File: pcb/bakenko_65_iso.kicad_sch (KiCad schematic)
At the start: 43 parts, among them J1 JST SH 4-pin, J2 Conn_01x02_MountingPin, Q1 AO3407A, SW1 SW_Omron_B3FS, U1 XC6206P302MR-G, U2 NRF52840 aQFN73, U3 MCP73831, X1 32MHz, X2 32.768KHz

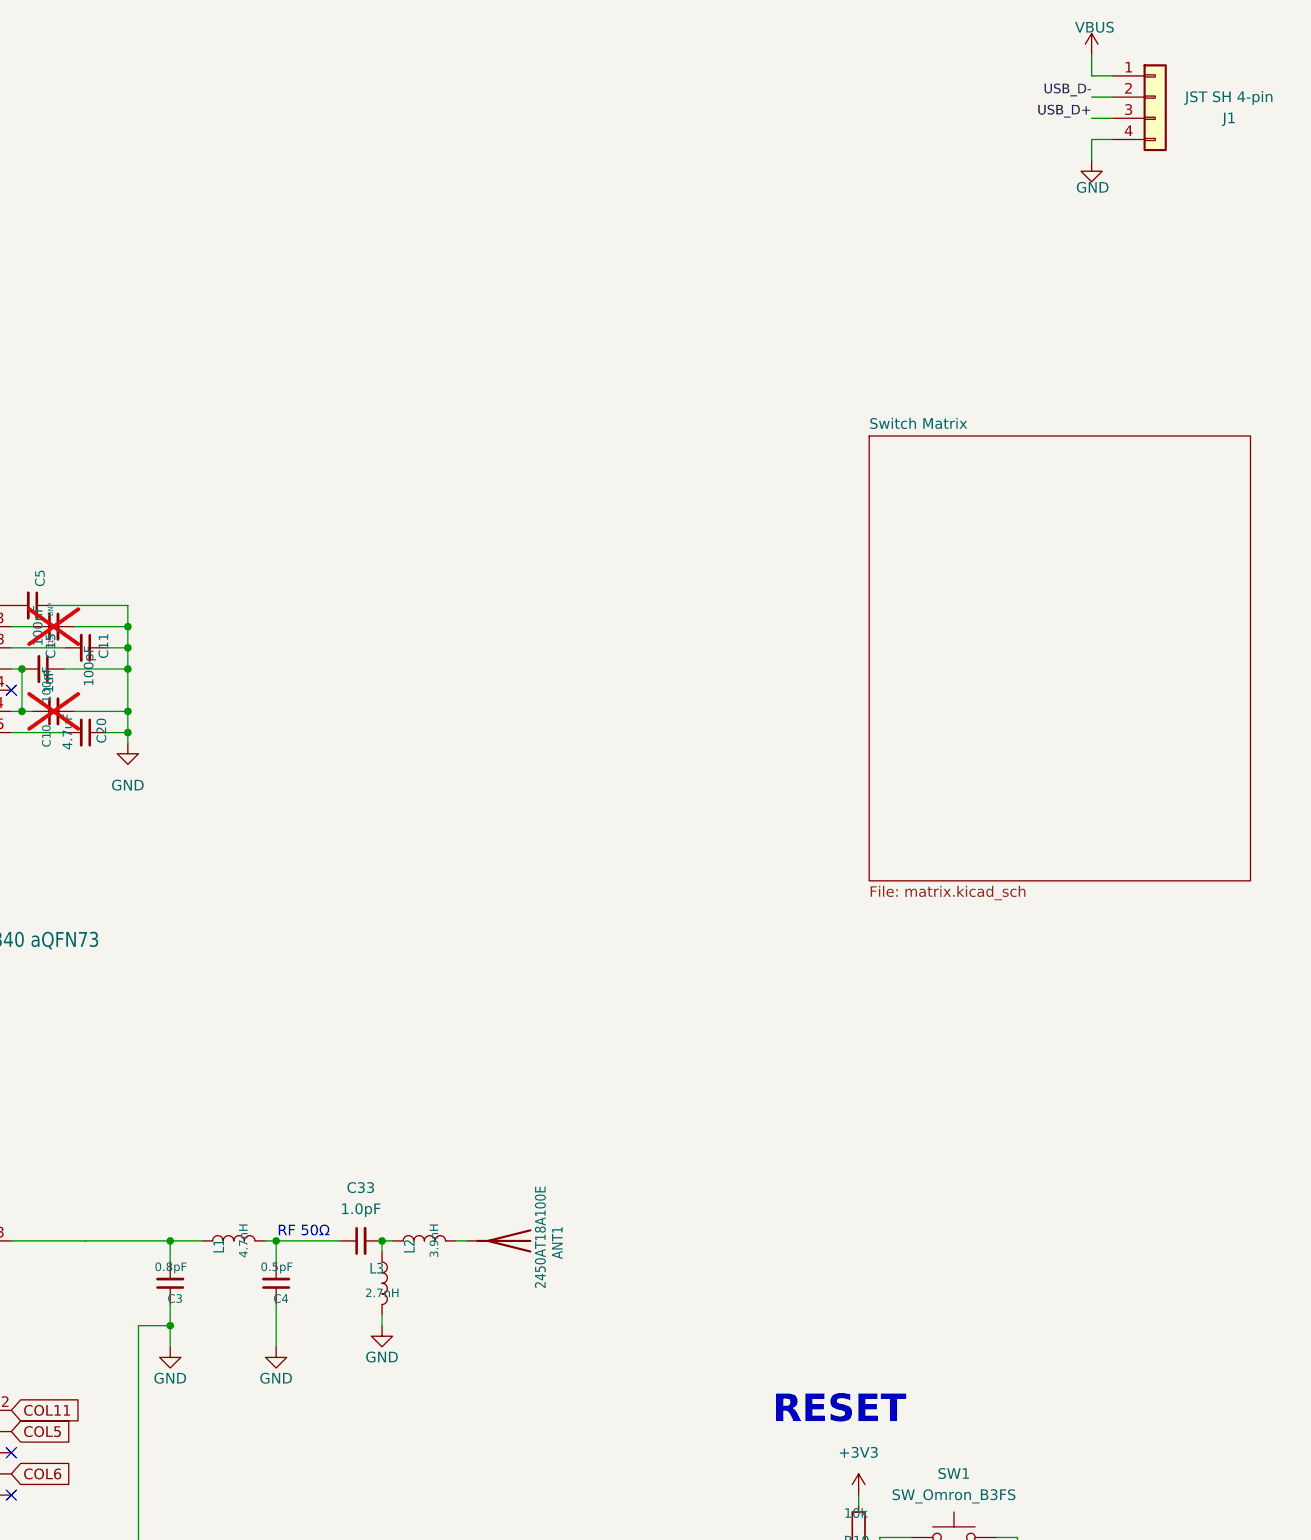
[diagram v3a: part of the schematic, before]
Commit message: Adding changes thanks to comment from devzone nordic
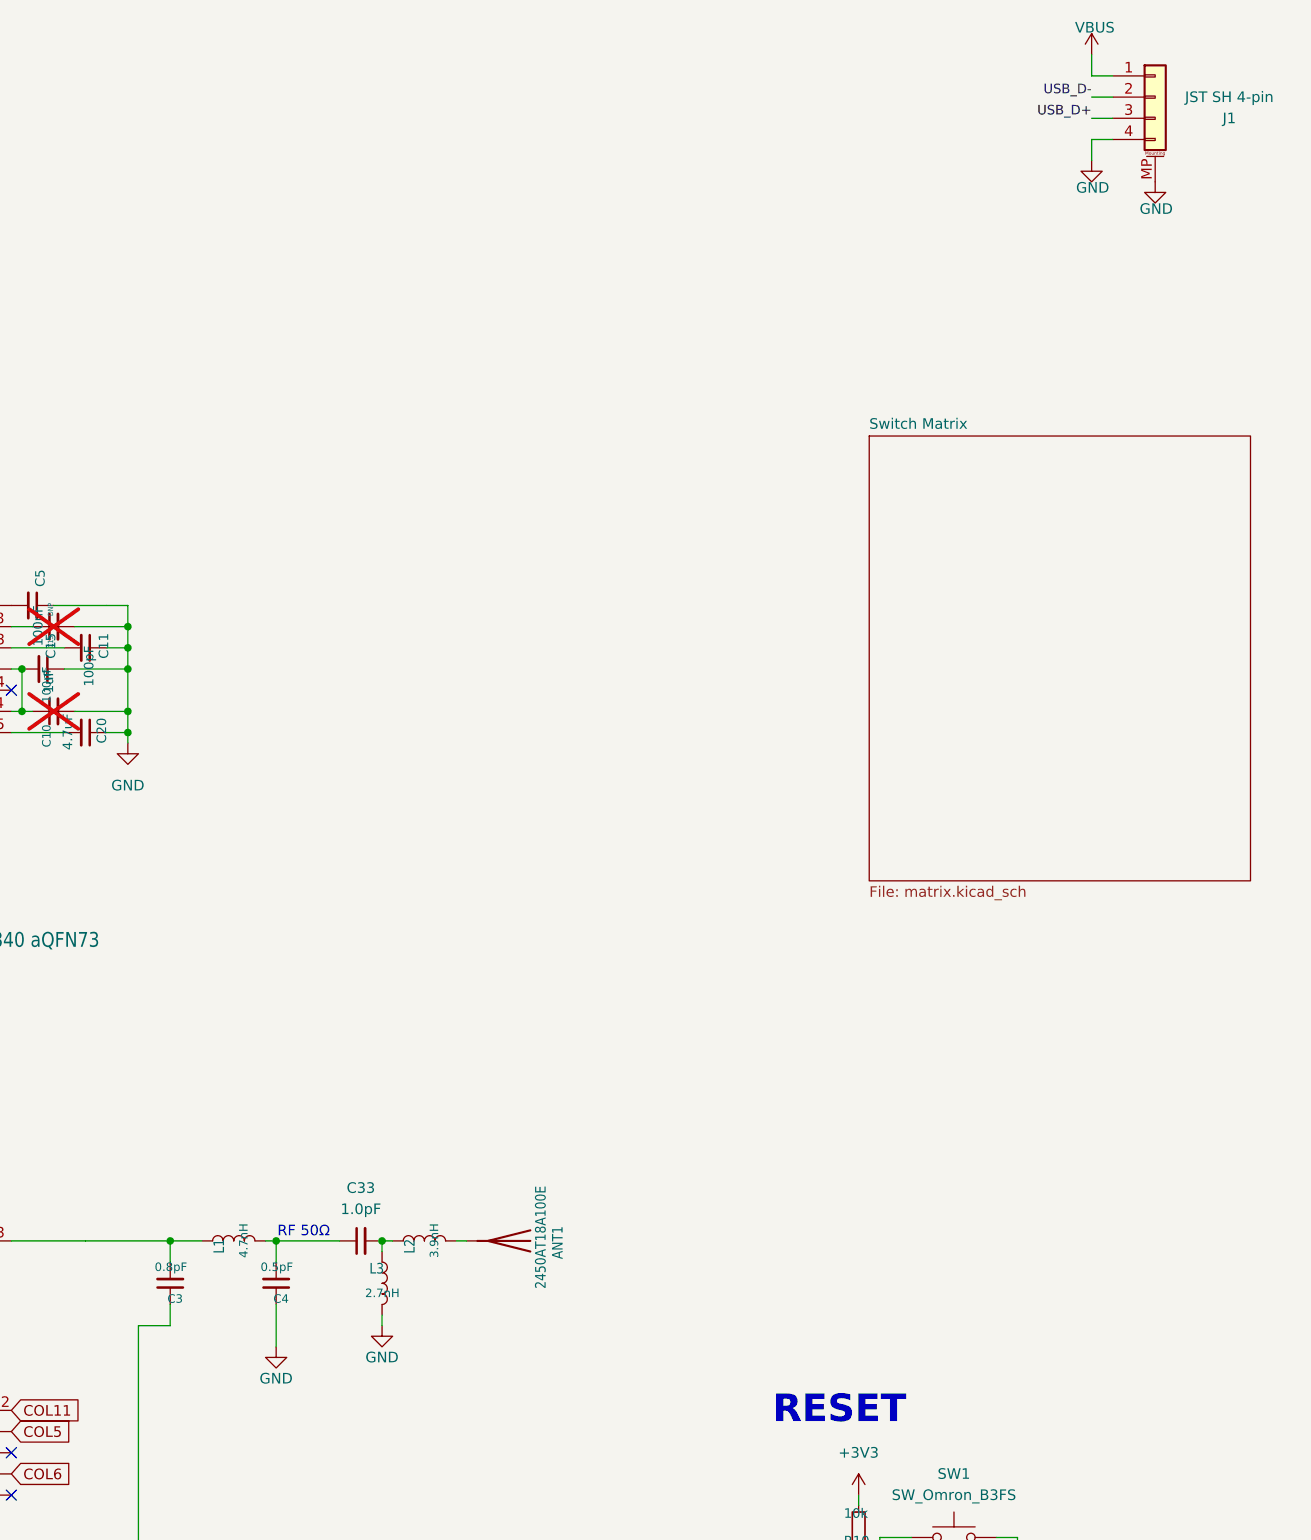
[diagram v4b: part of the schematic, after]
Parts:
- J1: footprint Connector_JST:JST_SH_SM04B-SRSS-TB_1x04-1MP_P1.00mm_Horizontal -> Connector_Molex:Molex_Pico-EZmate_78171-0004_1x04-1MP_P1.20mm_Vertical; symbol Connector_Generic:Conn_01x04 -> Connector_Generic_MountingPin:Conn_01x04_MountingPin; KiLib_Generator (none) -> connector/SMD_single_row_plus_mounting_pad
- J2: KiLib_Generator (none) -> connector/SMD_single_row_plus_mounting_pad
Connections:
- net GND: now also J1.MP (MountPin); no longer C3.1, U2.F23 (VSS_PA)
- new net: C3.1, U2.F23 (VSS_PA)
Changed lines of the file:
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@@
 	)
 	(junction
-		(at 267.97 194.31)
-		(diameter 0)
-		(color 0 0 0 0)
-	)
-	(junction
 		(at 194.31 88.9)
 		(diameter 0)
@@
 	(wire
 		(pts
-			(xy 267.97 194.31) (xy 267.97 196.85)
-		)
-		(stroke
-			(width 0)
-			(type default)
-		)
-	)
-	(wire
-		(pts
 			(xy 212.09 80.01) (xy 212.09 82.55)
 		)
@@
 	)
 	(symbol
-		(lib_id "Connector_Generic:Conn_01x04")
+		(lib_id "Connector_Generic_MountingPin:Conn_01x04_MountingPin")
 		(at 386.08 46.99 0)
 		(unit 1)
@@
 			)
 		)
-		(property "Footprint" "Connector_JST:JST_SH_SM04B-SRSS-TB_1x04-1MP_P1.00mm_Horizontal"
+		(property "Footprint" "Connector_Molex:Molex_Pico-EZmate_78171-0004_1x04-1MP_P1.20mm_Vertical"
 			(at 386.08 46.99 0)
 			(hide yes)
@@
 		(property "Description" ""
 			(at 386.08 46.99 0)
+			(hide yes)
 			(show_name no)
 			(do_not_autoplace no)
@@
 			)
 		)
+		(property "KiLib_Generator" "connector/SMD_single_row_plus_mounting_pad"
+			(at 386.08 46.99 0)
+			(hide yes)
+			(show_name no)
+			(do_not_autoplace no)
+			(effects
+				(font
+					(size 1.27 1.27)
+				)
+			)
+		)
 		(pin "1"
 		)
@@
 		(pin "4"
 		)
+		(pin "MP"
+		)
 		(instances
 			(project "bakenko_65_iso"
@@
 			)
 		)
-		(property "Description" "Generic connectable mounting pin connector, single row, 01x02, script generated (kicad-library-utils/schlib/autogen/connector/)"
+		(property "Description" ""
+			(at 114.3 166.37 0)
+			(hide yes)
+			(show_name no)
+			(do_not_autoplace no)
+			(effects
+				(font
+					(size 1.27 1.27)
+				)
+			)
+		)
+		(property "KiLib_Generator" "connector/SMD_single_row_plus_mounting_pad"
 			(at 114.3 166.37 0)
 			(hide yes)
@@
 	)
 	(symbol
-		(lib_name "GND_20")
-		(lib_id "power:GND")
-		(at 267.97 196.85 0)
-		(unit 1)
-		(body_style 1)
-		(exclude_from_sim no)
-		(in_bom yes)
-		(on_board yes)
-		(in_pos_files yes)
-		(dnp no)
-		(property "Reference" "#PWR028"
-			(at 267.97 203.2 0)
-			(hide yes)
-			(show_name no)
-			(do_not_autoplace no)
-			(effects
-				(font
-					(size 1.27 1.27)
-				)
-			)
-		)
-		(property "Value" "GND"
-			(at 267.97 200.66 0)
-			(show_name no)
-			(do_not_autoplace no)
-			(effects
-				(font
-					(size 1.27 1.27)
-				)
-			)
-		)
-		(property "Footprint" ""
-			(at 267.97 196.85 0)
-			(hide yes)
-			(show_name no)
-			(do_not_autoplace no)
-			(effects
-				(font
-					(size 1.27 1.27)
-				)
-			)
-		)
-		(property "Datasheet" ""
-			(at 267.97 196.85 0)
-			(hide yes)
-			(show_name no)
-			(do_not_autoplace no)
-			(effects
-				(font
-					(size 1.27 1.27)
-				)
-			)
-		)
-		(property "Description" "Power symbol creates a global label with name \"GND\" , ground"
-			(at 267.97 196.85 0)
-			(hide yes)
-			(show_name no)
-			(do_not_autoplace no)
-			(effects
-				(font
-					(size 1.27 1.27)
-				)
-			)
-		)
-		(pin "1"
-		)
-		(instances
-			(project "bakenko_65_iso"
-				(path "/287514b3-fc8e-4781-96ec-6e4b29b57f7d"
-					(reference "#PWR028")
-					(unit 1)
-				)
-			)
-		)
-	)
-	(symbol
 		(lib_id "Device:C_Small")
 		(at 171.45 128.27 180)
@@
 					(unit 1)
 				)
+			)
+		)
+	)
+	(symbol
+		(lib_id "power:GND")
+		(at 386.08 57.15 0)
+		(unit 1)
+		(body_style 1)
+		(exclude_from_sim no)
+		(in_bom yes)
+		(on_board yes)
+		(in_pos_files yes)
+		(dnp no)
+		(property "Reference" "#PWR03"
+			(at 386.08 63.5 0)
+			(hide yes)
+			(show_name no)
+			(do_not_autoplace no)
+			(effects
+				(font
+					(size 1.27 1.27)
+				)
+			)
+		)
+		(property "Value" "GND"
+			(at 386.207 60.4012 0)
+			(show_name no)
+			(do_not_autoplace no)
+			(effects
+				(font
+					(size 1.27 1.27)
+				)
+			)
+		)
+		(property "Footprint" ""
+			(at 386.08 57.15 0)
+			(hide yes)
+			(show_name no)
+			(do_not_autoplace no)
+			(effects
+				(font
+					(size 1.27 1.27)
+				)
+			)
+		)
+		(property "Datasheet" ""
+			(at 386.08 57.15 0)
+			(hide yes)
+			(show_name no)
+			(do_not_autoplace no)
+			(effects
+				(font
+					(size 1.27 1.27)
+				)
+			)
+		)
+		(property "Description" ""
+			(at 386.08 57.15 0)
+			(show_name no)
+			(do_not_autoplace no)
+			(effects
+				(font
+					(size 1.27 1.27)
+				)
+			)
+		)
+		(pin "1"
+		)
+		(instances
+			(project "bakenko_65_iso"
+				(path "/287514b3-fc8e-4781-96ec-6e4b29b57f7d"
+					(reference "#PWR03")
+					(unit 1)
+				)
